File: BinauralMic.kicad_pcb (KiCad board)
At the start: 2 copper layers, 60 parts, among them IC1 PCM2903CDBR, J1 RCJ-017, J2 USB4105-GF-A-120, J3 Conn_01x02_Pin, J4 Conn_01x02_Pin, U1 74LVC1G08, U2 MIC5504-3.3YM5, U3 TL972QDRQ1, X1 ECS-120-8-36-CKM-TR3

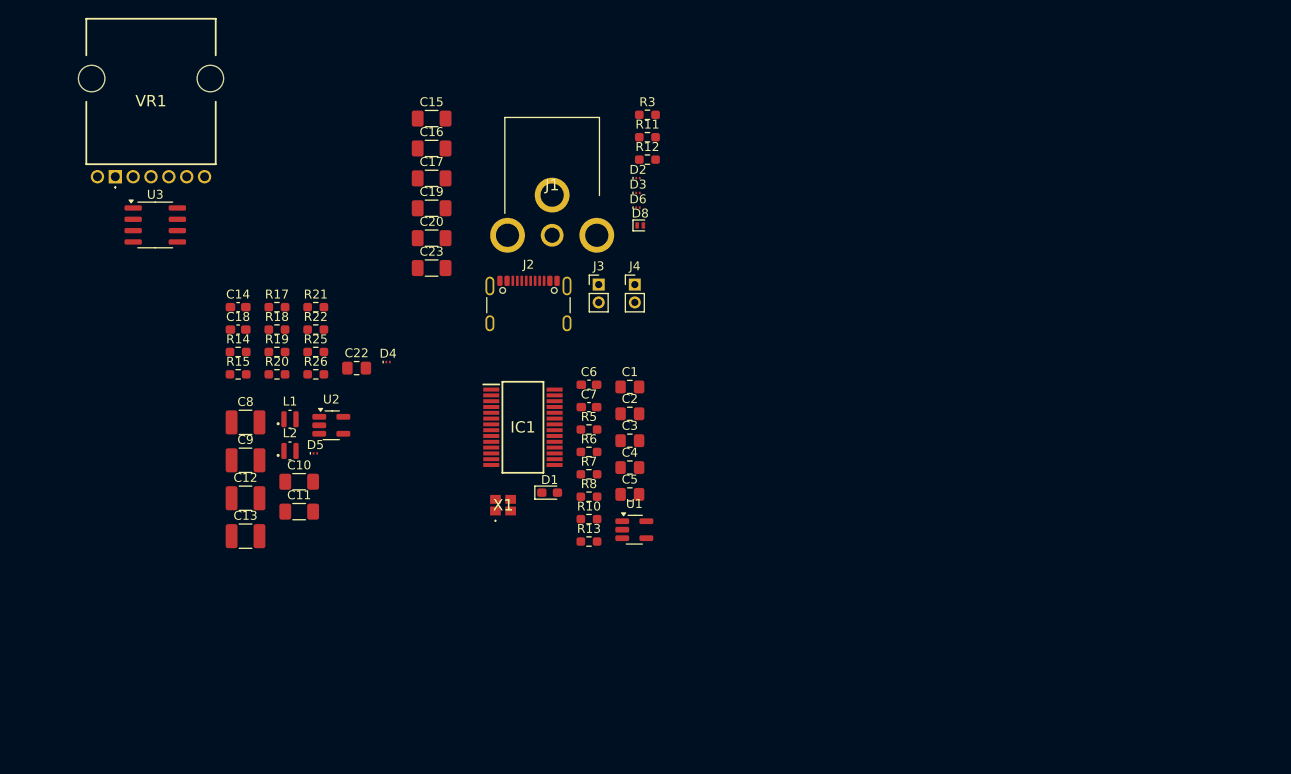
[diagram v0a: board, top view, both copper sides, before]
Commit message: Starting layout
Also why are the mf diodes so small
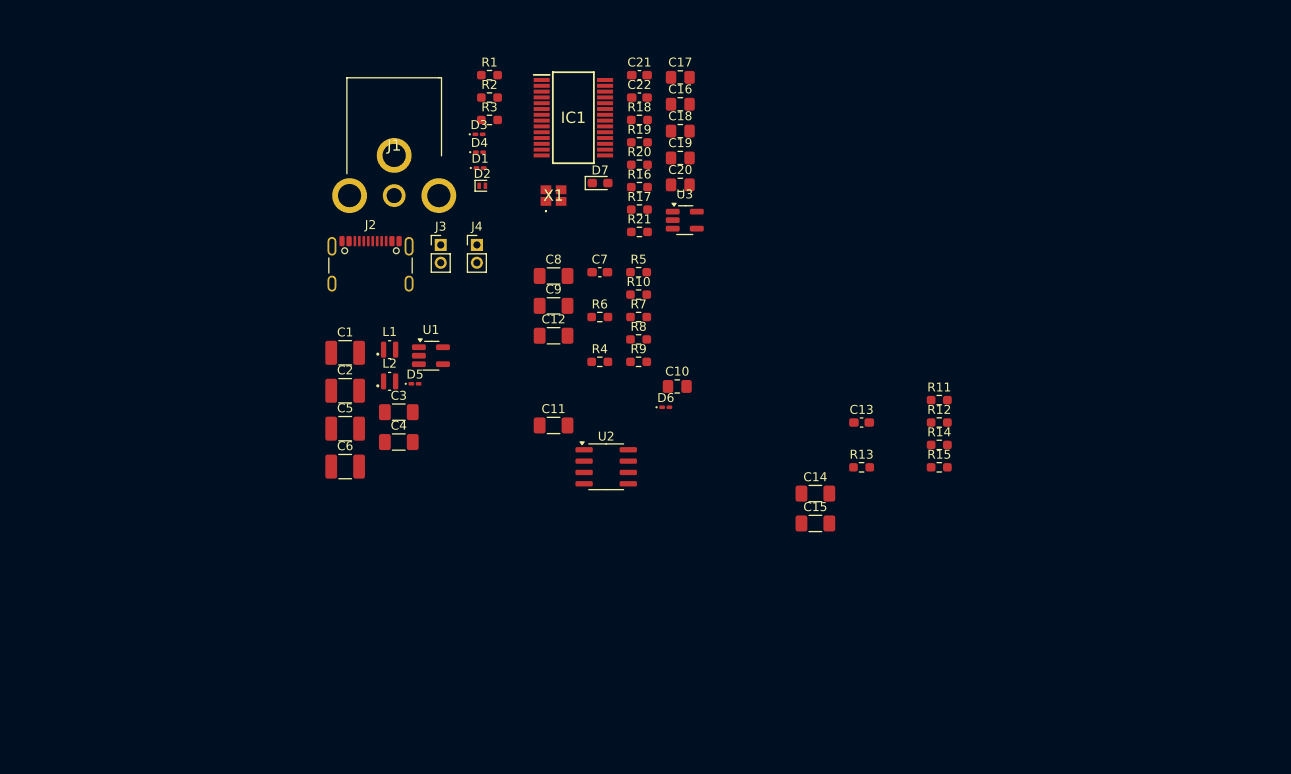
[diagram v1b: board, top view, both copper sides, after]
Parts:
- removed C23: 1u, Capacitor_SMD:C_1206_3216Metric_Pad1.33x1.80mm_HandSolder
- removed D8: PESD5V5C1BL, Diode_SMD:D_SOD-882
- removed R22: 5.9k, Resistor_SMD:R_0603_1608Metric_Pad0.98x0.95mm_HandSolder
- removed R25: 49.9, Resistor_SMD:R_0603_1608Metric_Pad0.98x0.95mm_HandSolder
- removed R26: 100k, Resistor_SMD:R_0603_1608Metric_Pad0.98x0.95mm_HandSolder
- removed VR1: P140KH1-Y20AR20K, binauralmic:P140KH1Y20AR20K
- added C21: 16p, Capacitor_SMD:C_0603_1608Metric_Pad1.08x0.95mm_HandSolder, F.Cu at (149.2, 54.6)
- added D7: LTST-C193KRKT-2A, LED_SMD:LED_0603_1608Metric_Pad1.05x0.95mm_HandSolder, F.Cu at (144.8, 66.7)
- added R1: 75, Resistor_SMD:R_0603_1608Metric_Pad0.98x0.95mm_HandSolder, F.Cu at (132.4, 54.6)
- added R16: 1.5k, Resistor_SMD:R_0603_1608Metric_Pad0.98x0.95mm_HandSolder, F.Cu at (149.2, 67.2)
- added R2: 5.1k, Resistor_SMD:R_0603_1608Metric_Pad0.98x0.95mm_HandSolder, F.Cu at (132.4, 57.1)
- added R4: 1M, Resistor_SMD:R_0603_1608Metric_Pad0.98x0.95mm_HandSolder, F.Cu at (144.8, 86.7)
- added R9: 100k, Resistor_SMD:R_0603_1608Metric_Pad0.98x0.95mm_HandSolder, F.Cu at (149.1, 86.7)
- C1, C5: value 10u -> 22u; footprint Capacitor_SMD:C_0805_2012Metric_Pad1.18x1.45mm_HandSolder -> Capacitor_SMD:C_1210_3225Metric_Pad1.33x2.70mm_HandSolder
- C10: value 1u -> 0.1u; footprint Capacitor_SMD:C_1206_3216Metric_Pad1.33x1.80mm_HandSolder -> Capacitor_SMD:C_0805_2012Metric_Pad1.18x1.45mm_HandSolder
- C12, C8, C9: value 22u -> 4.7u; footprint Capacitor_SMD:C_1210_3225Metric_Pad1.33x2.70mm_HandSolder -> Capacitor_SMD:C_1206_3216Metric_Pad1.33x1.80mm_HandSolder
- C13: value 22u -> 68p; footprint Capacitor_SMD:C_1210_3225Metric_Pad1.33x2.70mm_HandSolder -> Capacitor_SMD:C_0603_1608Metric_Pad1.08x0.95mm_HandSolder
- C14: value 68p -> 4.7u; footprint Capacitor_SMD:C_0603_1608Metric_Pad1.08x0.95mm_HandSolder -> Capacitor_SMD:C_1206_3216Metric_Pad1.33x1.80mm_HandSolder
- C16: value 4.7u -> 0.1u; footprint Capacitor_SMD:C_1206_3216Metric_Pad1.33x1.80mm_HandSolder -> Capacitor_SMD:C_0805_2012Metric_Pad1.18x1.45mm_HandSolder
- C17, C19, C20: value 4.7u -> 10u; footprint Capacitor_SMD:C_1206_3216Metric_Pad1.33x1.80mm_HandSolder -> Capacitor_SMD:C_0805_2012Metric_Pad1.18x1.45mm_HandSolder
- C18: value 68p -> 10u; footprint Capacitor_SMD:C_0603_1608Metric_Pad1.08x0.95mm_HandSolder -> Capacitor_SMD:C_0805_2012Metric_Pad1.18x1.45mm_HandSolder
- C2: value 0.1u -> 22u; footprint Capacitor_SMD:C_0805_2012Metric_Pad1.18x1.45mm_HandSolder -> Capacitor_SMD:C_1210_3225Metric_Pad1.33x2.70mm_HandSolder
- C22: value 0.1u -> 16p; footprint Capacitor_SMD:C_0805_2012Metric_Pad1.18x1.45mm_HandSolder -> Capacitor_SMD:C_0603_1608Metric_Pad1.08x0.95mm_HandSolder
- C3, C4: value 10u -> 1u; footprint Capacitor_SMD:C_0805_2012Metric_Pad1.18x1.45mm_HandSolder -> Capacitor_SMD:C_1206_3216Metric_Pad1.33x1.80mm_HandSolder
- C6: value 16p -> 22u; footprint Capacitor_SMD:C_0603_1608Metric_Pad1.08x0.95mm_HandSolder -> Capacitor_SMD:C_1210_3225Metric_Pad1.33x2.70mm_HandSolder
- C7: value 16p -> 68p
- D1: value LTST-C193KRKT-2A -> PESD3V3Y1BSF; footprint LED_SMD:LED_0603_1608Metric_Pad1.05x0.95mm_HandSolder -> Diode_SMD:D_0201_0603Metric_Pad0.64x0.40mm_HandSolder
- D2: value PESD3V3Y1BSF -> PESD5V5C1BL; footprint Diode_SMD:Nexperia_DSN0603-2_0.6x0.3mm_P0.4mm -> Diode_SMD:D_SOD-882
- D3, D4, D5, D6: footprint Diode_SMD:Nexperia_DSN0603-2_0.6x0.3mm_P0.4mm -> Diode_SMD:D_0201_0603Metric_Pad0.64x0.40mm_HandSolder
- R10: value 1M -> 100k
- R11: value 5.1k -> 1M
- R12: value 5.1k -> 5.9k
- R13: value 1M -> 18k
- R14: value 1M -> 49.9
- R15: value 5.9k -> 100k
- R17: value 100k -> 1M
- R18: value 49.9 -> 5.6k
- R19, R20: value 100k -> 22
- R3: value 75 -> 5.1k
- R5: value 5.6k -> 5.9k
- R6: value 22 -> 18k
- R7: value 22 -> 49.9
- R8: value 1.5k -> 100k
- U1: value 74LVC1G08 -> MIC5504-3.3YM5
- U2: value MIC5504-3.3YM5 -> TL972QDRQ1; footprint Package_TO_SOT_SMD:SOT-23-5_HandSoldering -> Package_SO:SOIC-8_3.9x4.9mm_P1.27mm
- U3: value TL972QDRQ1 -> 74LVC1G08; footprint Package_SO:SOIC-8_3.9x4.9mm_P1.27mm -> Package_TO_SOT_SMD:SOT-23-5_HandSoldering
- moved R14 79.2 mm to (182.8, 96.0)
- moved R15 79.2 mm to (182.8, 98.6)
- moved C13 70.2 mm to (174.1, 93.5)
- moved C14 68.0 mm to (168.9, 101.5)
- moved C15 62.5 mm to (168.9, 104.8)
- moved U3 59.3 mm to (154.3, 70.9)
- moved C18 54.3 mm to (153.8, 60.9)
- moved R19 46.9 mm to (149.2, 62.1)
- moved R18 46.9 mm to (149.2, 59.6)
- moved R20 46.9 mm to (149.2, 64.7)
- moved R12 44.0 mm to (182.8, 93.5)
- moved R11 44.0 mm to (182.8, 91.0)
- moved C22 43.8 mm to (149.2, 57.1)
- moved C10 43.7 mm to (153.5, 89.5)
- moved R17 42.1 mm to (149.2, 69.7)
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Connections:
- C1 pad 1: VDD -> /VBUS
- C10 pad 1: +5V -> VCC
- C12 pad 1: VCC -> GND
- C12 pad 2: GND -> /VCOM
- C13 pad 1: VDD -> /Mic Preamp/VN_{R}
- C13 pad 2: GND -> /Mic Preamp/VOUT_{R}
- C14 pad 1: /Mic Preamp/VN_{L} -> /VRAW_{R}
- C14 pad 2: /Mic Preamp/VOUT_{L} -> /Mic Preamp/VN_{R}
- C15 pad 1: /VRAW_{L} -> /Mic Preamp/VOUT_{R}_R
- C15 pad 2: /Mic Preamp/VN_{L} -> /VIN_{R}
- C16 pad 1: /Mic Preamp/VOUT_{L}_R -> GND
- C16 pad 2: /VIN_{L} -> VDD
- C17 pad 1: GND -> VDD
- C17 pad 2: /VCOM -> GND
- C18 pad 1: /Mic Preamp/VN_{R} -> VCC
- C18 pad 2: /Mic Preamp/VOUT_{R} -> GND
- C19 pad 1: /VRAW_{R} -> GND
- C19 pad 2: /Mic Preamp/VN_{R} -> /VCOM
- C2 pad 1: GND -> +5V
- C2 pad 2: VDD -> GND
- C20 pad 1: /Mic Preamp/VOUT_{R}_R -> VCC
- C20 pad 2: /VIN_{R} -> GND
- C22 pad 1: VCC -> /USB ADC/XTO
- C3 pad 1: VCC -> +5V
- C4 pad 1: GND -> VCC
- C4 pad 2: /VCOM -> GND
- C6 pad 1: /USB ADC/XTI -> VDD
- C7 pad 1: /USB ADC/XTO -> /Mic Preamp/VN_{L}
- C7 pad 2: GND -> /Mic Preamp/VOUT_{L}
- C8 pad 1: /VBUS -> /VRAW_{L}
- C8 pad 2: GND -> /Mic Preamp/VN_{L}
- C9 pad 1: +5V -> /Mic Preamp/VOUT_{L}_R
- C9 pad 2: GND -> /VIN_{L}
- D1 pad 1: /USB ADC/~{SSPND}_R -> GND
- D1 pad 2: VDD -> /Connectors/DOUT_R
- D2 pad 2: /D+ -> /VBUS
- D3 pad 2: /D- -> /D+
- D4 pad 2: VCC -> /D-
- D6 pad 2: /Connectors/DOUT_R -> VCC
- R10 pad 1: /VBUS -> /VCOM
- R11 pad 1: /Connectors/CC1 -> /Mic Preamp/VN_{R}
- R11 pad 2: GND -> /Mic Preamp/VOUT_{R}
- R12 pad 1: /Connectors/CC2 -> +5V
- R12 pad 2: GND -> /VRAW_{R}
- R13 pad 1: /USB ADC/XTI -> /Mic Preamp/VN_{R}
- R13 pad 2: /USB ADC/XTO -> /Mic Preamp/VOUT_{R}
- R14 pad 1: /Mic Preamp/VN_{L} -> /Mic Preamp/VOUT_{R}
- R14 pad 2: /Mic Preamp/VOUT_{L} -> /Mic Preamp/VOUT_{R}_R
- R15 pad 1: +5V -> /VIN_{R}
- R15 pad 2: /VRAW_{L} -> GND
- R17 pad 1: /VCOM -> /VBUS
- R18 pad 1: /Mic Preamp/VOUT_{L} -> /USB ADC/~{SSPND}_R
- R18 pad 2: /Mic Preamp/VOUT_{L}_R -> /USB ADC/~{SSPND}
- R19 pad 1: /VIN_{L} -> /D+
- R19 pad 2: GND -> /USB ADC/D+_R
- R20 pad 1: VCC -> /D-
- R20 pad 2: /VCOM -> /USB ADC/D-_R
- R21 pad 1: /Mic Preamp/VN_{R} -> /USB ADC/XTI
- R21 pad 2: /Mic Preamp/VOUT_{R} -> /USB ADC/XTO
- R3 pad 1: /DOUT -> /Connectors/CC2
- R3 pad 2: /Connectors/DOUT_R -> GND
- R5 pad 1: /USB ADC/~{SSPND}_R -> +5V
- R5 pad 2: /USB ADC/~{SSPND} -> /VRAW_{L}
- R6 pad 1: /D+ -> /Mic Preamp/VN_{L}
- R6 pad 2: /USB ADC/D+_R -> /Mic Preamp/VOUT_{L}
- R7 pad 1: /D- -> /Mic Preamp/VOUT_{L}
- R7 pad 2: /USB ADC/D-_R -> /Mic Preamp/VOUT_{L}_R
- R8 pad 1: /USB ADC/D+_PUR -> /VIN_{L}
- R8 pad 2: /D+ -> GND
- U1 pad 1: VDD -> +5V
- U1 pad 2: /VBUS -> GND
- U1 pad 3: GND -> +5V
- U1 pad 4: /USB ADC/D+_PUR -> unconnected-(U1-NC-Pad4)
- U1 pad 5: VDD -> VCC
- U2 pad 1: +5V -> /Mic Preamp/VOUT_{L}
- U2 pad 2: GND -> /Mic Preamp/VN_{L}
- U2 pad 3: +5V -> /VCOM
- U2 pad 4: unconnected-(U2-NC-Pad4) -> GND
- U2 pad 5: VCC -> /VCOM
- U3 pad 1: /Mic Preamp/VOUT_{L} -> VDD
- U3 pad 2: /Mic Preamp/VN_{L} -> /VBUS
- U3 pad 3: /VCOM -> GND
- U3 pad 4: GND -> /USB ADC/D+_PUR
- U3 pad 5: /VCOM -> VDD

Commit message: Started layout?
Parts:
- R2, R3: moved to B.Cu
- moved R3 37.6 mm to (104.0, 84.2), turned to 180 degrees
- moved R2 37.4 mm to (104.0, 81.5), turned to 180 degrees
- moved C1 26.7 mm to (96.6, 103.8), turned to -90 degrees
- moved L1 26.6 mm to (98.6, 99.2)
- moved C2 20.9 mm to (100.6, 103.8), turned to -90 degrees
- moved J2 16.8 mm to (103.4, 82.9), turned to -90 degrees
- moved L2 16.2 mm to (108.8, 99.2)
- moved C5 11.0 mm to (110.8, 103.8), turned to -90 degrees
- moved C6 10.9 mm to (106.8, 103.8), turned to -90 degrees

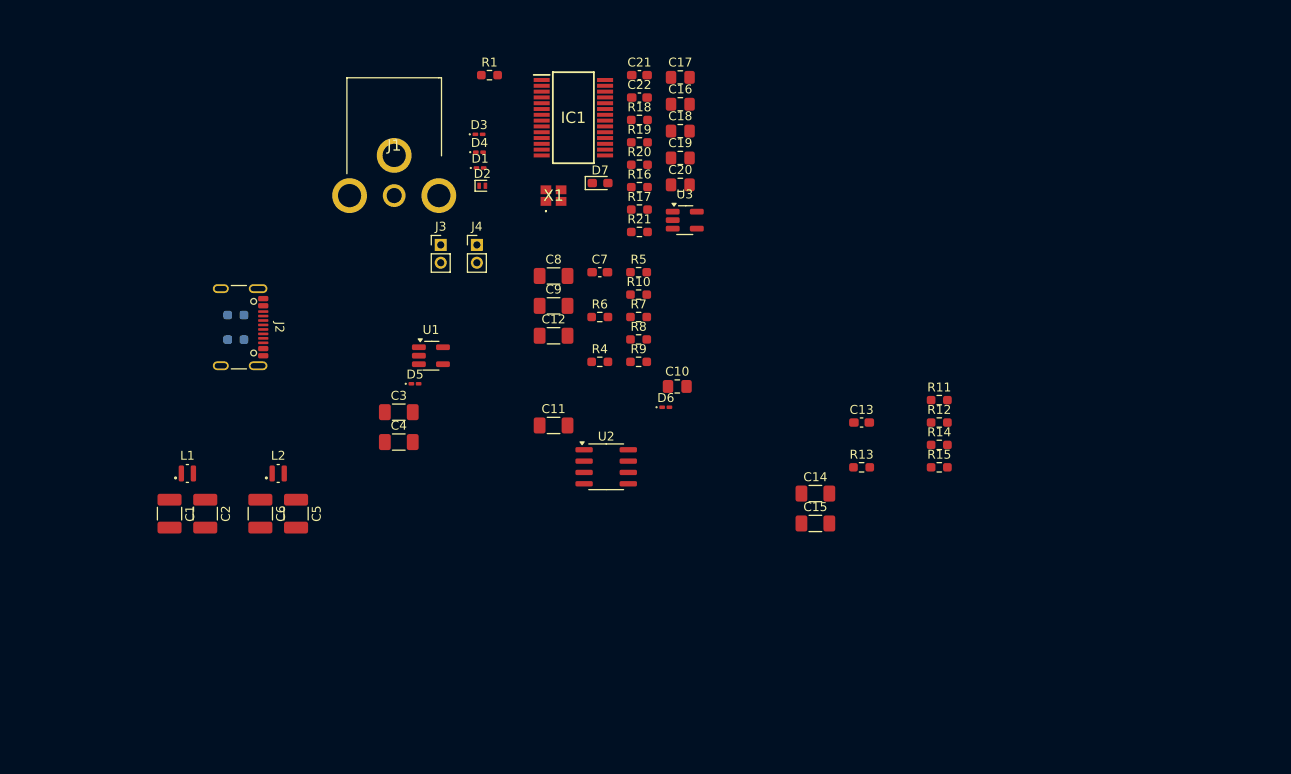
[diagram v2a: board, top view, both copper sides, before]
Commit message: Reannotated schematic + restarted layout
woohoo
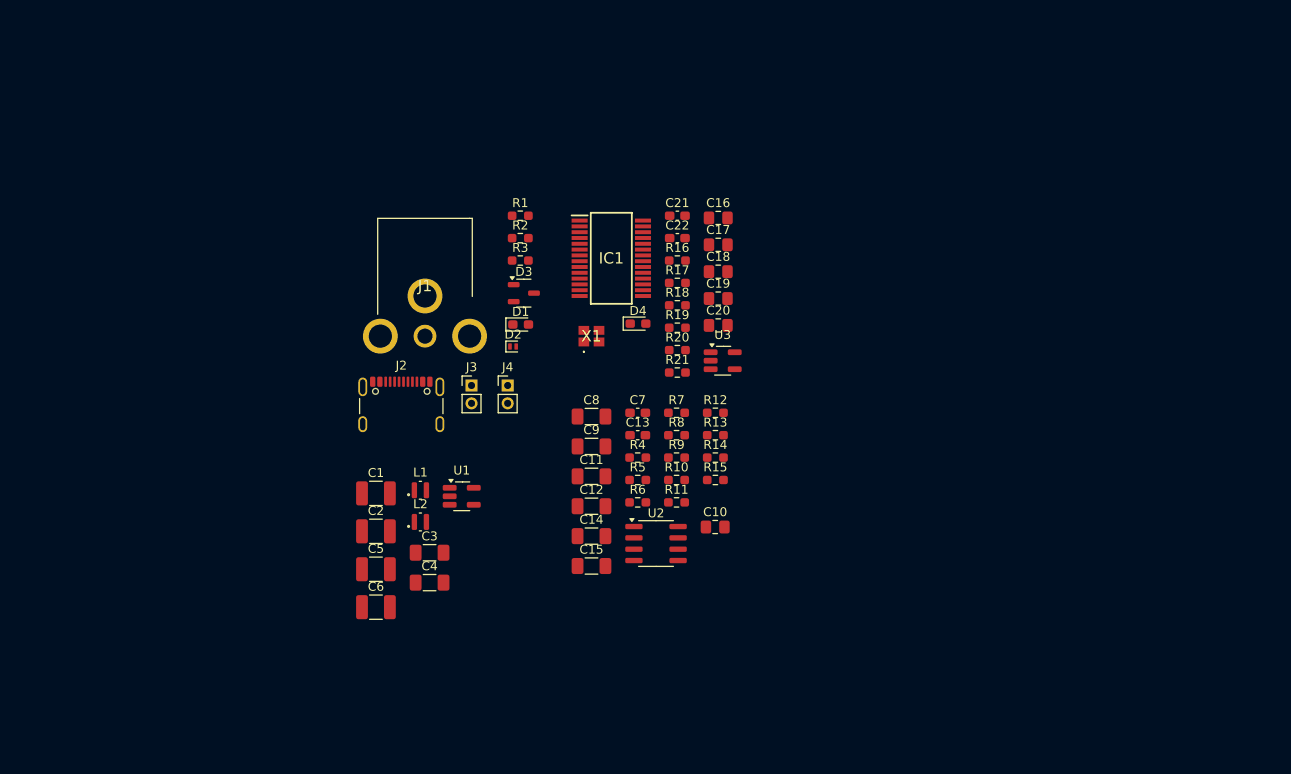
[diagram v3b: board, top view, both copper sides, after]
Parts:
- removed D5, D6: PESD3V3Y1BSF, Diode_SMD:D_0201_0603Metric_Pad0.64x0.40mm_HandSolder
- removed D7: LTST-C193KRKT-2A, LED_SMD:LED_0603_1608Metric_Pad1.05x0.95mm_HandSolder
- D1: value PESD3V3Y1BSF -> CG0603MLU-3.3E; footprint Diode_SMD:D_0201_0603Metric_Pad0.64x0.40mm_HandSolder -> Diode_SMD:D_0603_1608Metric_Pad1.05x0.95mm_HandSolder
- D3: value PESD3V3Y1BSF -> PESD2USB3UVT-QR; footprint Diode_SMD:D_0201_0603Metric_Pad0.64x0.40mm_HandSolder -> Package_TO_SOT_SMD:SOT-23-3
- D4: value PESD3V3Y1BSF -> LTST-C193KRKT-2A; footprint Diode_SMD:D_0201_0603Metric_Pad0.64x0.40mm_HandSolder -> LED_SMD:LED_0603_1608Metric_Pad1.05x0.95mm_HandSolder
- R2, R3: moved to F.Cu
- moved R3 33.1 mm to (135.9, 75.4), turned to 0 degrees
- moved R2 33.0 mm to (135.9, 72.9), turned to 0 degrees
- moved R11 31.6 mm to (153.4, 102.5)
- moved L1 26.2 mm to (124.7, 101.1)
- moved D4 26.2 mm to (149.1, 82.5)
- moved C15 25.5 mm to (143.9, 109.6)
- moved C14 25.5 mm to (143.9, 106.3)
- moved C13 25.1 mm to (149.0, 95.0)
- moved R14 25.1 mm to (157.7, 97.5)
- moved R15 25.1 mm to (157.7, 100.0)
- moved R12 25.1 mm to (157.7, 92.5)
- moved R5 23.3 mm to (149.0, 100.0)
- moved C1 23.2 mm to (119.7, 101.5), turned to 0 degrees
- moved J2 21.5 mm to (122.5, 92.7), turned to 0 degrees
- moved R10 21.2 mm to (153.4, 100.0)
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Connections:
- D3 pad 1: GND -> /D+
- D3 pad 2: /D+ -> /D-
- D4 pad 1: GND -> /USB ADC/~{SSPND}_R
- D4 pad 2: /D- -> VDD

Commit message: Add more detailed RCJ-014 model + shifting things around
Also added another ESD diode for VBUS because only one will be connected for USB C :/
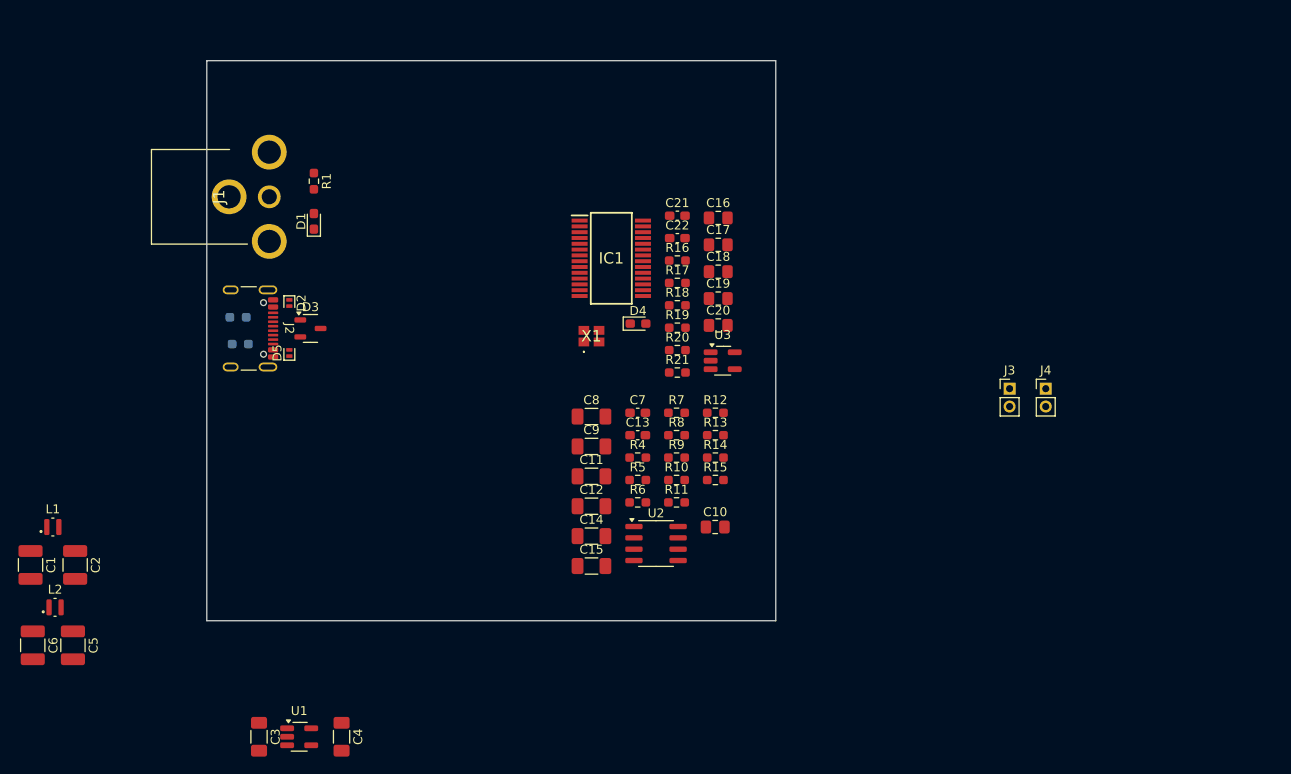
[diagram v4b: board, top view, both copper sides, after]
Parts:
- added D5: PESD5V5C1BL, Diode_SMD:D_SOD-882, F.Cu at (110.0, 85.8)
- R2, R3: moved to B.Cu
- moved J3 60.3 mm to (190.7, 89.8)
- moved J4 60.3 mm to (194.8, 89.8)
- moved L2 42.0 mm to (83.8, 114.2)
- moved L1 41.4 mm to (83.5, 105.2)
- moved C1 39.5 mm to (81.0, 109.5), turned to -90 degrees
- moved C6 38.7 mm to (81.2, 118.5), turned to -90 degrees
- moved C5 35.0 mm to (85.8, 118.5), turned to -90 degrees
- moved C2 33.9 mm to (86.0, 109.5), turned to -90 degrees
- moved R2 32.8 mm to (104.2, 81.8), turned to 180 degrees
- moved R3 32.7 mm to (104.5, 84.8), turned to 180 degrees
- moved U1 32.5 mm to (111.1, 128.8)
- moved C3 28.1 mm to (106.6, 128.8), turned to -90 degrees
- moved D1 25.9 mm to (112.8, 71.0), turned to 90 degrees
- moved D2 25.5 mm to (110.0, 80.2), turned to -90 degrees
- moved D3 24.2 mm to (112.4, 83.0)
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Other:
- board outline added: 63.8 x 62.8 mm
- copper layers 2 -> 4
